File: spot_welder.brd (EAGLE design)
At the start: 75.5 x 51 mm, 38 parts, among them IC1 ATMEGA328PU, IC2 7805L, IC3 MOC3052M, T1 BT151-800R, T2 BT151-800R, Y1 16MHZ

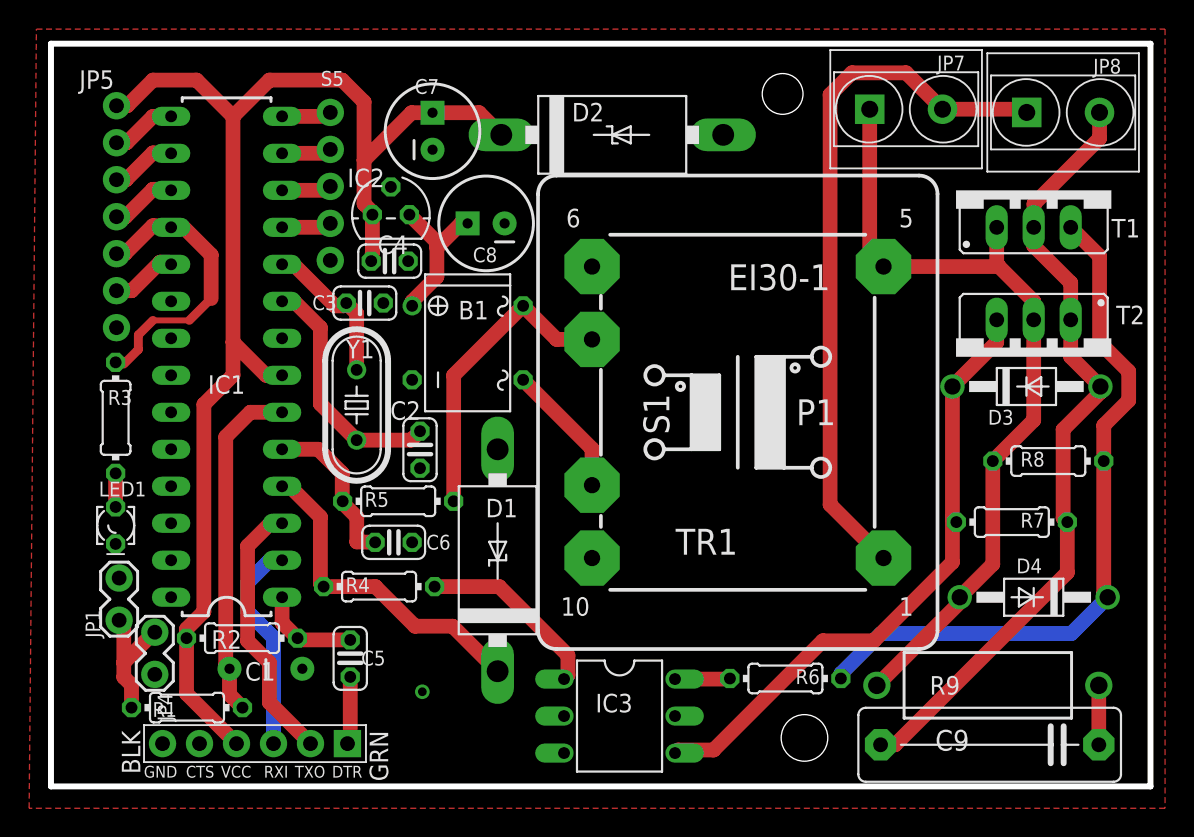
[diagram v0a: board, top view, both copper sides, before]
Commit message: limited ground plane to low-voltage part; fixed angles on traces
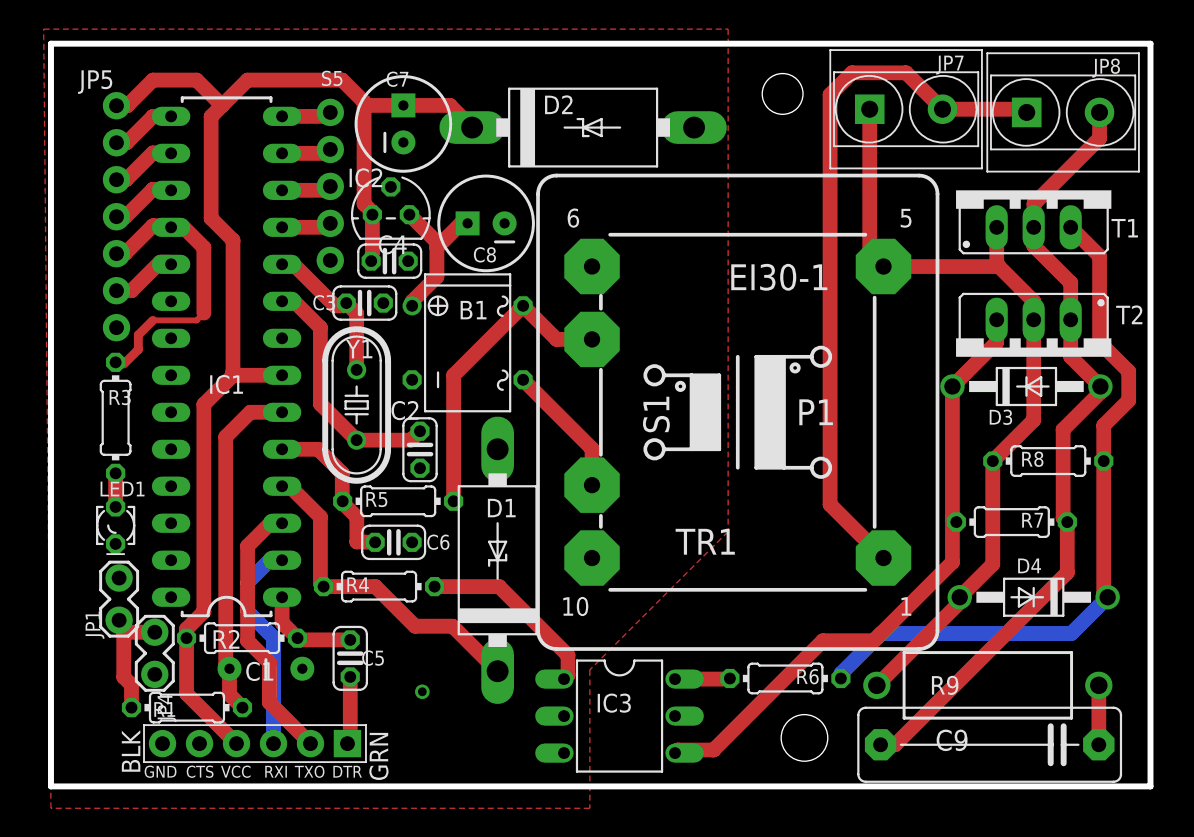
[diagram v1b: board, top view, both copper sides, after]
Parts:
- moved D2 2.06 mm to (63.0, 79.2)
- moved C7 2.06 mm to (50.7, 79.5)
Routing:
- net VCC: track 93.1 -> 90.1 mm
- net N$21: track 9.35 -> 8.48 mm
